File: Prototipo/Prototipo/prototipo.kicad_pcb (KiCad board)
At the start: 2 copper layers, 148 parts, among them Q11_1 MMBT2222A, Q11_2 MMBT2907A, Q11_3 MMBT2222A, Q12_1 MMBT2222A, Q12_2 MMBT2907A, Q12_3 MMBT2222A, Q1_1 MMBT2222A, Q1_2 MMBFJ201, Q21_1 MMBT2222A, Q21_2 MMBT2907A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

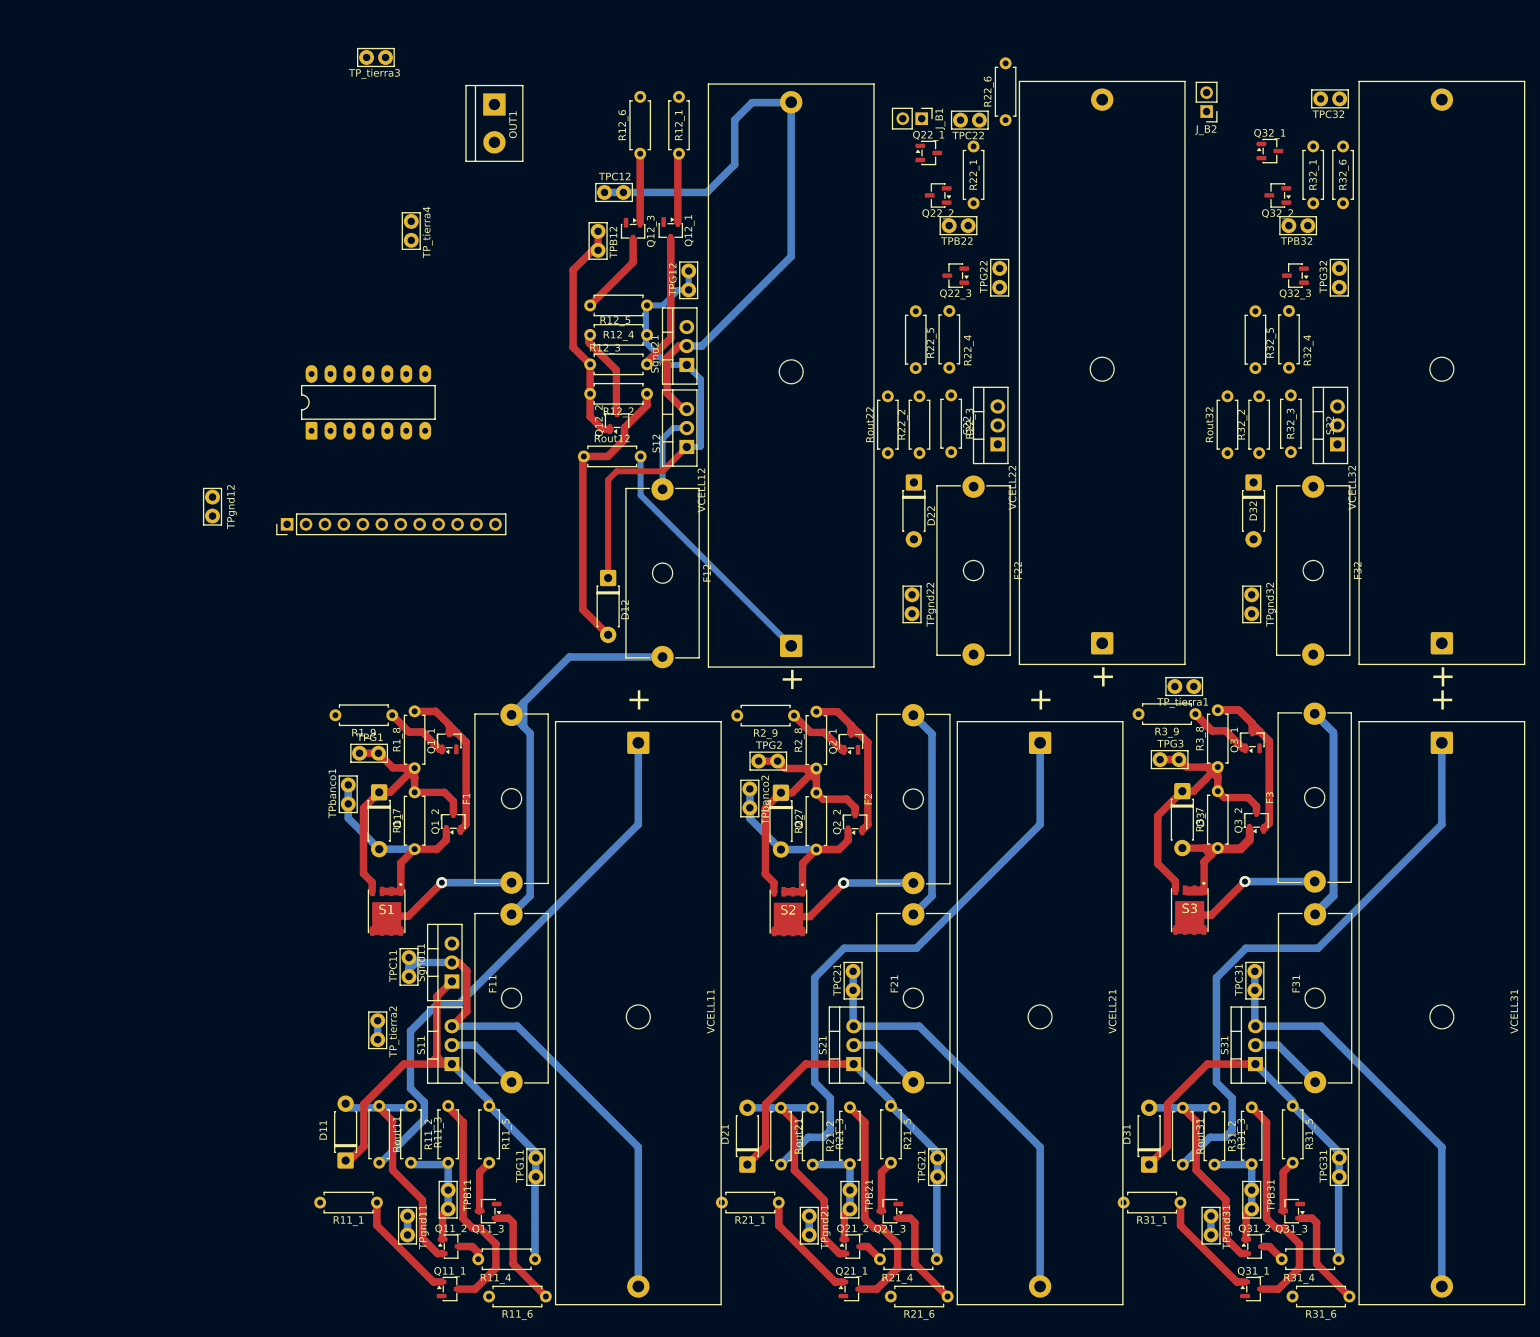
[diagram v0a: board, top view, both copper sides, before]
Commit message: conexiones internas de todas las celdas
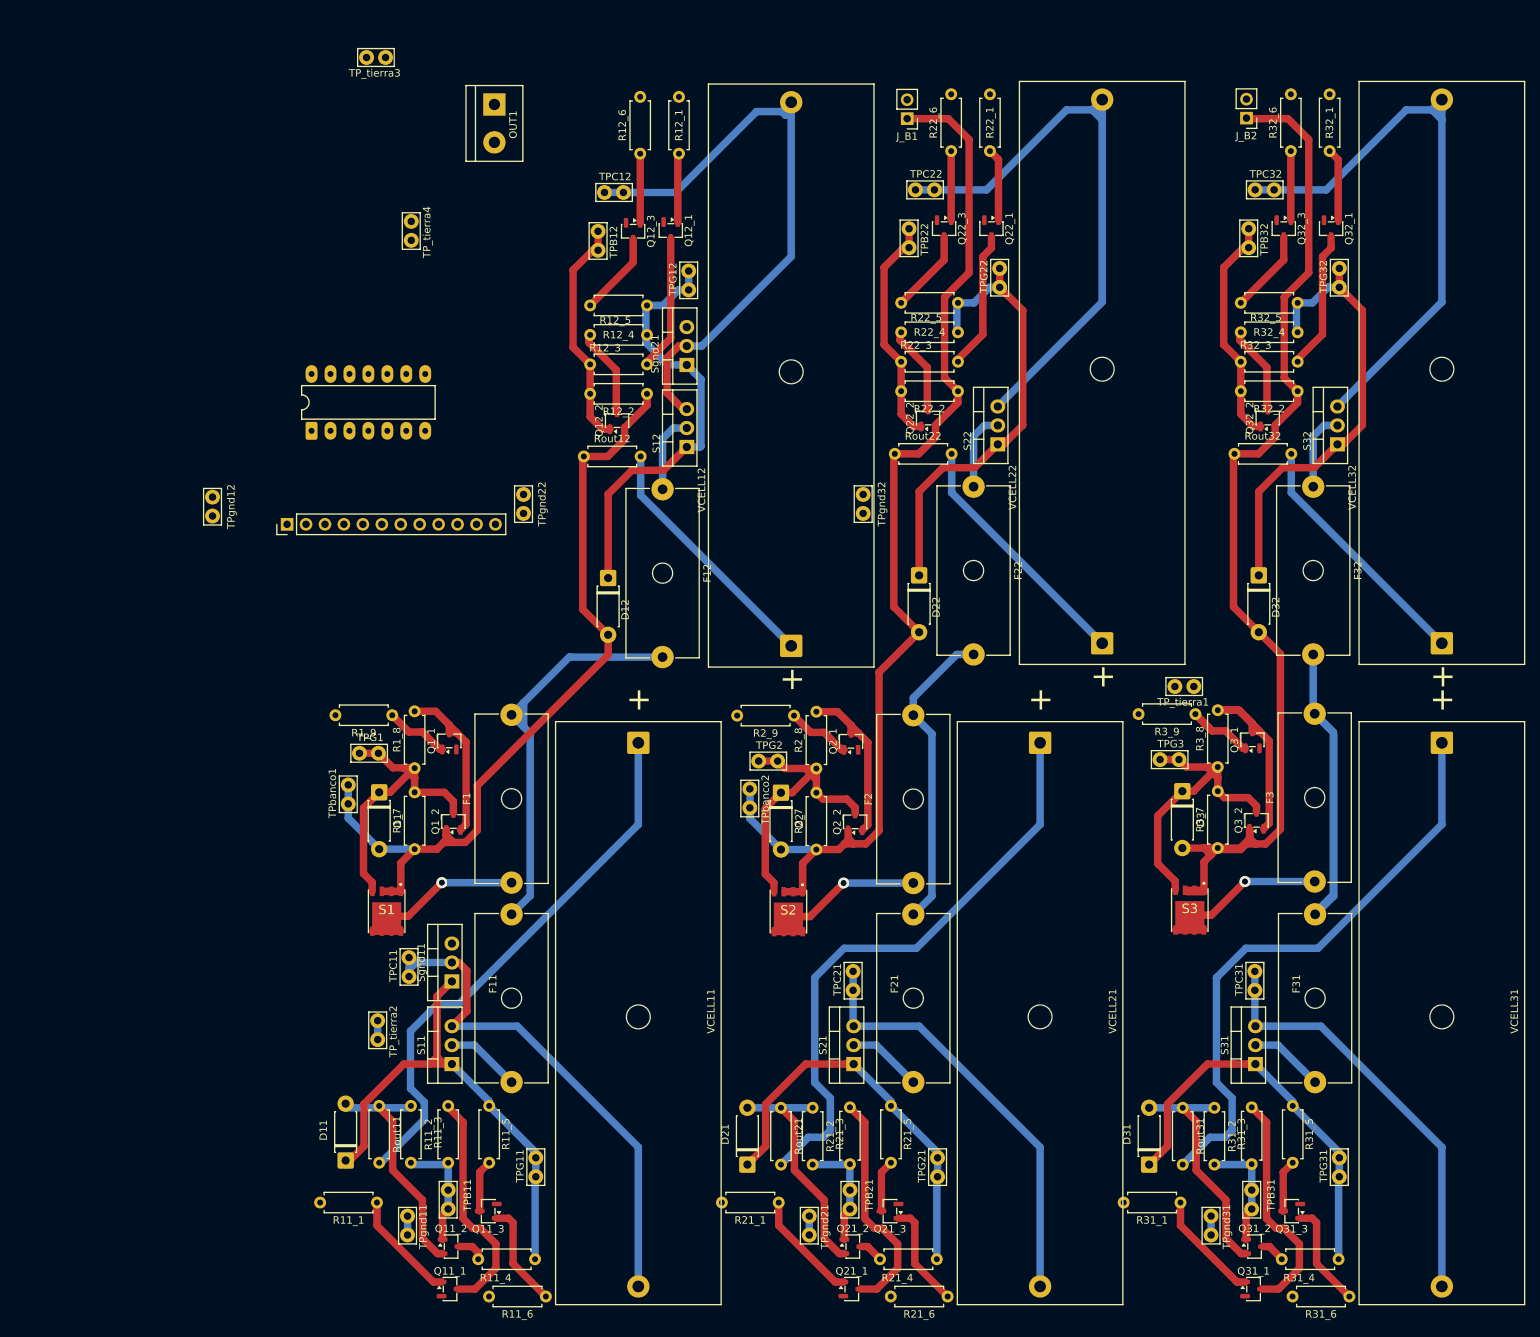
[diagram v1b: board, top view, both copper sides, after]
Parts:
- moved TPgnd32 53.8 mm to (432.2, 206.0)
- moved TPgnd22 53.8 mm to (386.7, 206.0)
- moved Q22_2 29.9 mm to (440.9, 193.2), turned to 90 degrees
- moved Q32_2 29.9 mm to (486.4, 193.2), turned to 90 degrees
- moved TPC32 13.7 mm to (487.3, 162.6), turned to 180 degrees
- moved Q32_1 13.2 mm to (494.9, 167.8), turned to -90 degrees
- moved Q22_1 13.2 mm to (449.4, 167.8), turned to -90 degrees
- moved D22 12.5 mm to (439.7, 214.3)
- moved D32 12.5 mm to (485.2, 214.3)
- moved TPC22 9.98 mm to (441.8, 162.6), turned to 180 degrees
- moved R32_6 9.90 mm to (489.6, 157.4)
- moved R22_2 9.77 mm to (444.9, 189.6), turned to 180 degrees
- moved R32_2 9.77 mm to (490.5, 189.6), turned to 180 degrees
- moved R22_6 8.39 mm to (444.0, 157.4)
- moved R32_3 8.08 mm to (482.8, 185.7), turned to 0 degrees
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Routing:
- net /celda_21/bus_pos: track 119.4 -> 247.0 mm
- net /celda_31/bus_pos: track 61.6 -> 180.2 mm
- net /celda_32/cell_neg: track 0.00 -> 78.9 mm
- net /celda_22/cell_neg: track 0.00 -> 78.9 mm
- net /celda_32/gate: track 0.00 -> 61.9 mm
- net /celda_22/gate: track 0.00 -> 61.9 mm
- net /celda_11/bus_pos: track 130.1 -> 183.7 mm
- net Net-(VCELL32-+): track 0.00 -> 33.8 mm
- net Net-(VCELL22-+): track 0.00 -> 33.8 mm
- net Net-(Q22_2-B): track 0.00 -> 30.9 mm
- net Net-(Q32_2-B): track 0.00 -> 30.9 mm
- net Net-(Q32_1-C): track 0.00 -> 18.6 mm
- net Net-(Q22_1-C): track 0.00 -> 18.6 mm
- net Net-(Q32_2-C): track 0.00 -> 12.1 mm
- net Net-(Q22_2-C): track 0.00 -> 12.1 mm
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
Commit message: celdas superiores conectadas a la entrada
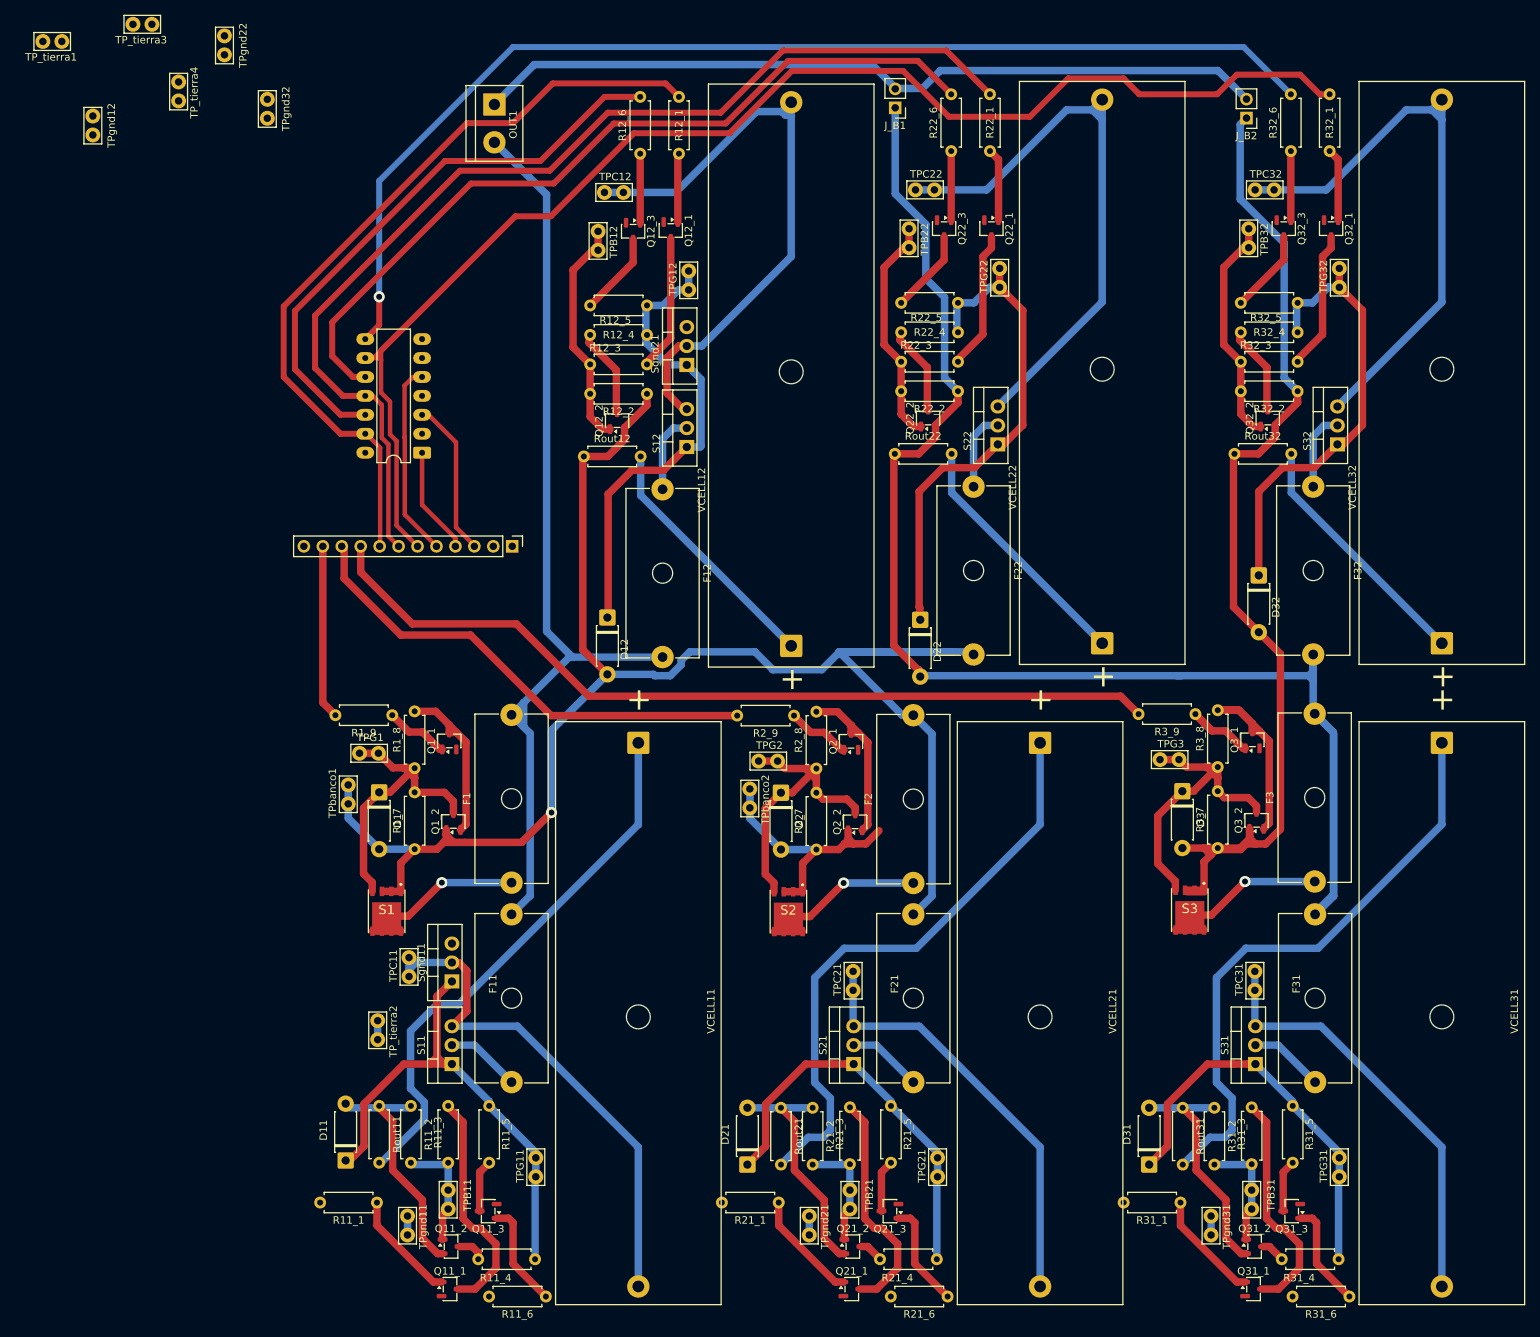
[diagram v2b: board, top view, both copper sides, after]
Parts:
- moved TP_tierra1 174.7 mm to (322.2, 142.7)
- moved TPgnd32 95.9 mm to (352.3, 153.0)
- moved TPgnd22 73.4 mm to (346.6, 144.5)
- moved TPgnd12 53.6 mm to (328.9, 155.2)
- moved TP_tierra4 36.4 mm to (340.4, 150.7)
- moved TP_tierra3 31.6 mm to (334.3, 140.4)
- moved IN1 30.3 mm to (385.1, 210.4), turned to -90 degrees
- moved A1 15.1 mm to (373.1, 197.8), turned to 180 degrees
- moved D22 5.95 mm to (439.9, 220.2)
- moved D12 5.30 mm to (397.9, 219.9)
- moved J_B1 2.16 mm to (436.5, 151.6)
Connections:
- IN1 pad 11: Vc3 -> Vc1
- IN1 pad 3: Vc_11 -> Vc_21
- IN1 pad 4: Vc_21 -> Vc_11
- IN1 pad 9: Vc1 -> Vc3
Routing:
- net Vc_32: track 0.00 -> 183.6 mm
- net /celda_32/Vcontrol_neg: track 0.00 -> 154.3 mm, vias 0 -> 1
- net Vc_22: track 0.00 -> 145.6 mm
- net Vc3: track 0.00 -> 115.7 mm
- net /celda_22/Vcontrol_neg: track 0.00 -> 109.5 mm
- net Net-(J_B1-Pin_2): track 0.00 -> 107.1 mm
- net Vc_12: track 0.00 -> 105.7 mm
- net /celda_12/Vcontrol_neg: track 0.00 -> 78.0 mm
- net /celda_11/bus_neg: track 55.5 -> 128.9 mm
- net /celda_11/bus_pos: track 183.7 -> 256.7 mm, vias 0 -> 1
- net Vc2: track 0.00 -> 64.8 mm
- net /celda_21/bus_pos: track 247.0 -> 277.2 mm
- net Vc_31: track 0.00 -> 26.2 mm
- net Vc1: track 0.00 -> 23.4 mm
- net Vc_21: track 0.00 -> 21.0 mm
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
